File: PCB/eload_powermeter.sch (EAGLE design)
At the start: 78 parts, among them IC1 ADS1115_IC, IC2 SGM8582, IC3 TP4056, IC4 FS312F-G, IC5 MT3608, IC6 FS8205, K2 TXD2SA-4.5V, Q1 BSS123, Q3 BSS123, Q4 IRF520, Q5 BSS123, Q6 IRF520, Q7 IRF520, U1 ATMEGA328P, Y1 16MHz

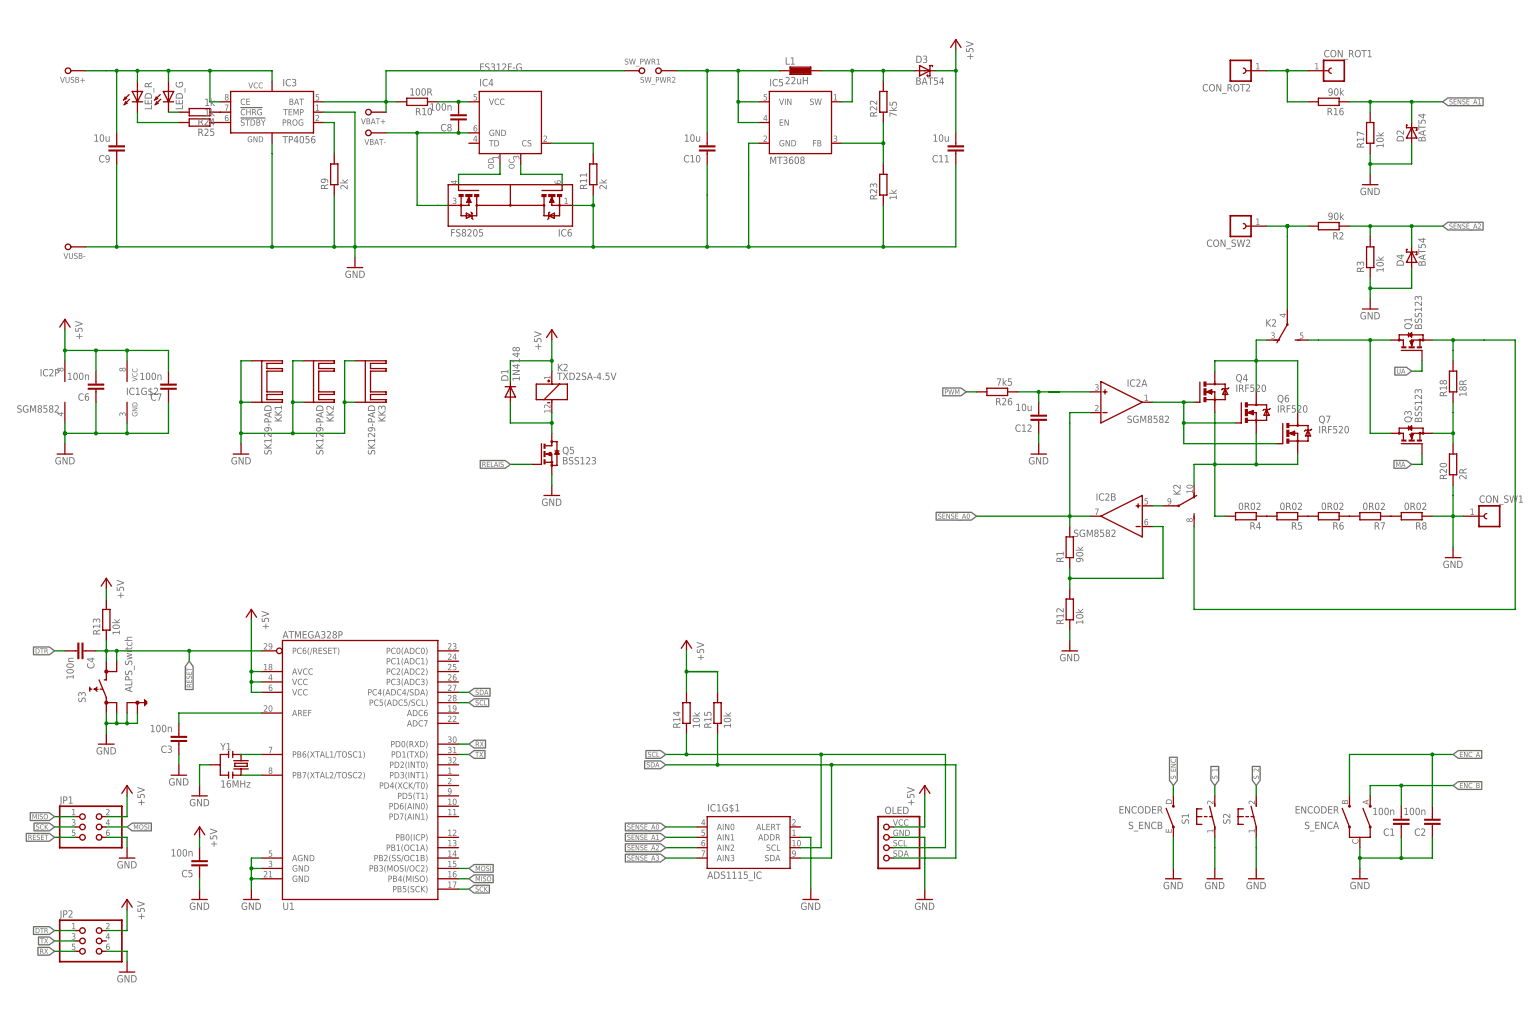
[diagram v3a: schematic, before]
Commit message: Finish Layout, document schematic with blocks
Routing the last connections of the layout. Starting with the naming on the top panel.
Documenting the schematic by adding functional blocks and descriping them.
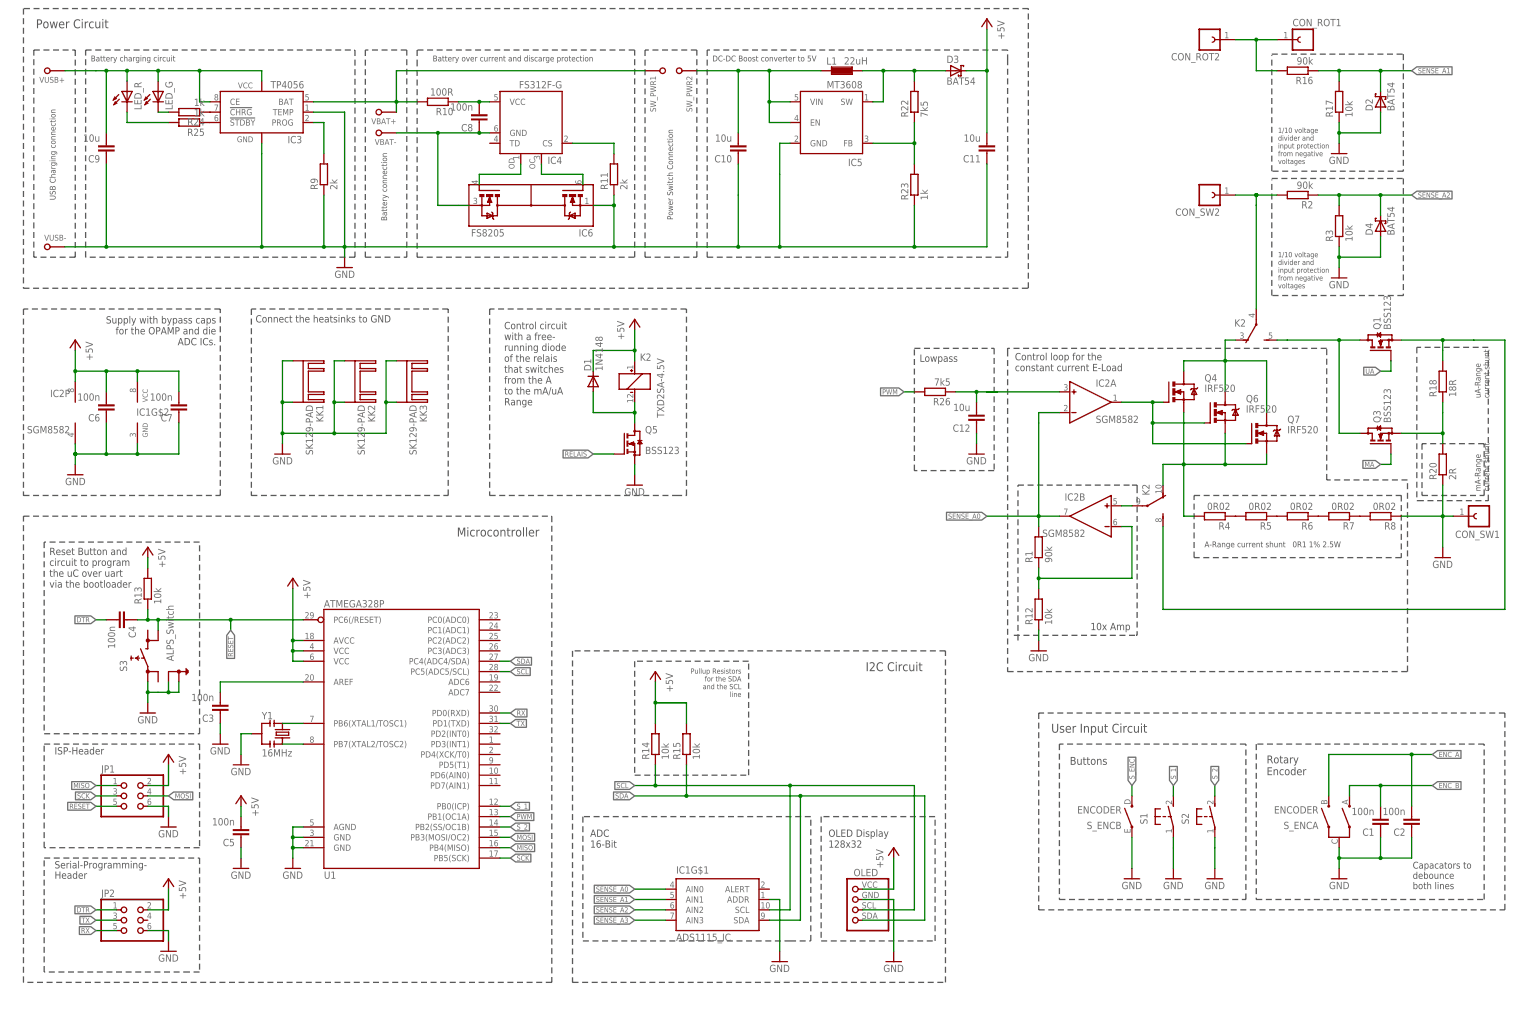
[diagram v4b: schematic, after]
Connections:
- net GND: no longer S3.3.2
- net PWM: now also U1.PB1(OC1A)
- net RESET: no longer S3.4.1
- net S_1: now also U1.PB0(ICP)
- net S_2: now also U1.PB2(SS/OC1B)
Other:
- note added: "1/10 voltage divider and input protection from negative voltages"
- note added: "10x Amp"
- note added: "A-Range current shunt 0R1 1% 2.5W"
- note added: "ADC 16-Bit"
- note added: "Battery charging circuit"
- note added: "Battery connection"
- note added: "Battery over current and discarge protection"
- note added: "Buttons"
- note added: "Capacators to debounce both lines"
- note added: "Connect the heatsinks to GND"
- note added: "Control circuit with a free- running diode of the relais that switches from the A to the mA/uA Range"
- note added: "Control loop for the constant current E-Load"
- note added: "DC-DC Boost converter to 5V"
- note added: "Header"
- note added: "I2C Circuit"
- note added: "ISP-Header"
- note added: "Lowpass"
- note added: "Microcontroller"
- note added: "OLED Display 128x32"
- note added: "Power Circuit"
- note added: "Power Switch Connection"
- note added: "Pullup Resistors for the SDA and the SCL line"
- note added: "Reset Button and circuit to program the uC over uart via the bootloader"
- note added: "Rotary Encoder"
- note added: "Serial-Programming-"
- note added: "Supply with bypass caps for the OPAMP and die ADC ICs."
- note added: "USB Charging connection"
- note added: "User Input Circuit"
- note added: "mA-Range current shunt"
- note added: "uA-Range current shunt"
- moved on the sheet: C1, C10, C11, C12, C2, C3, C4, C5, C6, C7, C8, C9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

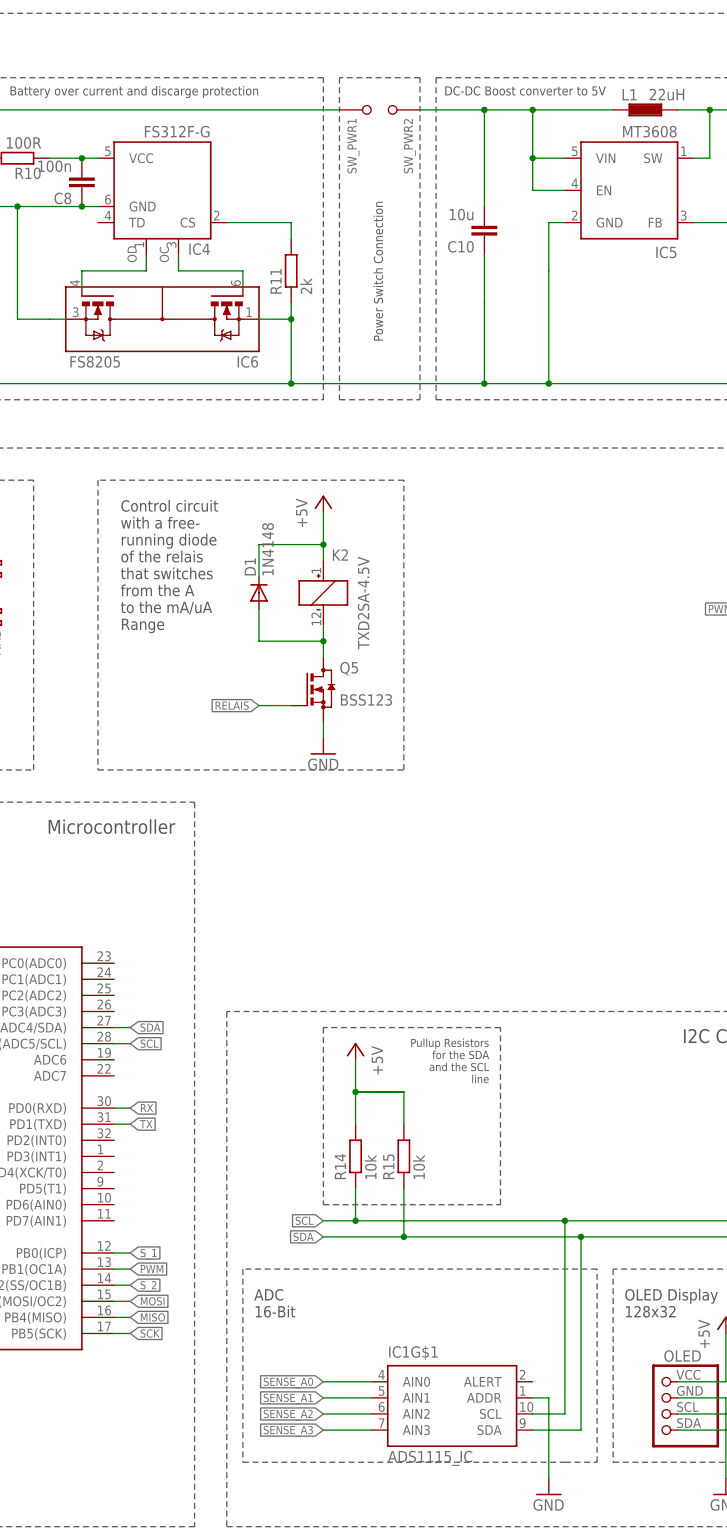
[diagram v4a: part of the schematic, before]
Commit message: Adding some missing uC connections.
Adding some connections of the uC that were missing before.
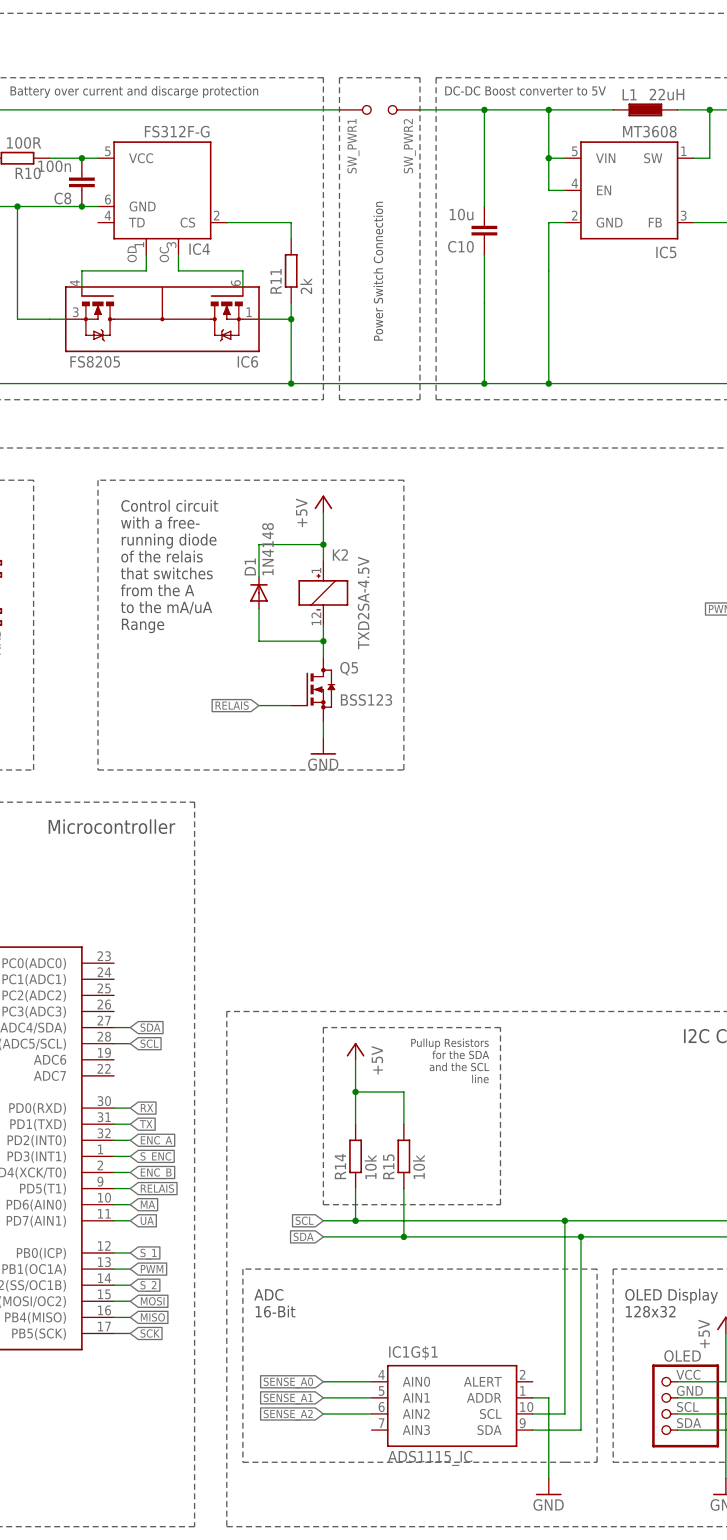
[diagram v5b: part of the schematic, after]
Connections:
- removed net SENSE_A3: IC1G$1.AIN3
- net ENC_A: now also U1.PD2(INT0)
- net ENC_B: now also U1.PD4(XCK/T0)
- net MA: now also U1.PD6(AIN0)
- net RELAIS: now also U1.PD5(T1)
- net S_ENC: now also U1.PD3(INT1)
- net UA: now also U1.PD7(AIN1)
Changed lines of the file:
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@@
 <wire x1="48.26" y1="25.4" x2="48.26" y2="22.86" width="0.1524" layer="91"/>
+</segment>
+<segment>
+<junction x="25.4" y="142.24"/>
 </segment>
 </net>
@@
 <wire x1="167.64" y1="81.28" x2="175.26" y2="81.28" width="0.1524" layer="91"/>
 <pinref part="R15" gate="G$1" pin="2"/>
-<wire x1="175.26" y1="81.28" x2="167.64" y2="81.28" width="0.1524" layer="91"/>
 <wire x1="175.26" y1="76.2" x2="175.26" y2="81.28" width="0.1524" layer="91"/>
 <junction x="167.64" y="81.28"/>
@@
 <wire x1="347.98" y1="162.56" x2="345.44" y2="162.56" width="0.1524" layer="91"/>
 </segment>
+<segment>
+<pinref part="U1" gate="G$1" pin="PD7(AIN1)"/>
+<wire x1="129.54" y1="60.96" x2="132.08" y2="60.96" width="0.1524" layer="91"/>
+<label x="132.08" y="60.96" size="1.27" layer="95" xref="yes"/>
+</segment>
 </net>
 <net name="MA" class="0">
@@
 <wire x1="347.98" y1="139.7" x2="345.44" y2="139.7" width="0.1524" layer="91"/>
 <label x="345.44" y="139.7" size="1.27" layer="95" rot="R180" xref="yes"/>
+</segment>
+<segment>
+<pinref part="U1" gate="G$1" pin="PD6(AIN0)"/>
+<wire x1="129.54" y1="63.5" x2="132.08" y2="63.5" width="0.1524" layer="91"/>
+<label x="132.08" y="63.5" size="1.27" layer="95" xref="yes"/>
 </segment>
 </net>
@@
 </segment>
 </net>
-<net name="SENSE_A3" class="0">
-<segment>
-<wire x1="170.18" y1="27.94" x2="162.56" y2="27.94" width="0.1524" layer="91"/>
-<pinref part="IC1" gate="G$1" pin="AIN3"/>
-<label x="162.56" y="27.94" size="1.27" layer="95" rot="R180" xref="yes"/>
-</segment>
-</net>
 <net name="SENSE_A2" class="0">
 <segment>
@@
 <label x="152.4" y="142.24" size="1.27" layer="95" rot="R180" xref="yes"/>
 </segment>
+<segment>
+<pinref part="U1" gate="G$1" pin="PD5(T1)"/>
+<wire x1="129.54" y1="66.04" x2="132.08" y2="66.04" width="0.1524" layer="91"/>
+<label x="132.08" y="66.04" size="1.27" layer="95" xref="yes"/>
+</segment>
 </net>
 <net name="ENC_B" class="0">
@@
 <label x="358.14" y="60.96" size="1.27" layer="95" xref="yes"/>
 </segment>
+<segment>
+<pinref part="U1" gate="G$1" pin="PD4(XCK/T0)"/>
+<wire x1="129.54" y1="68.58" x2="132.08" y2="68.58" width="0.1524" layer="91"/>
+<label x="132.08" y="68.58" size="1.27" layer="95" xref="yes"/>
+</segment>
 </net>
 <net name="ENC_A" class="0">
@@
 <label x="358.14" y="68.58" size="1.27" layer="95" xref="yes"/>
 </segment>
+<segment>
+<pinref part="U1" gate="G$1" pin="PD2(INT0)"/>
+<wire x1="129.54" y1="73.66" x2="132.08" y2="73.66" width="0.1524" layer="91"/>
+<label x="132.08" y="73.66" size="1.27" layer="95" xref="yes"/>
+</segment>
 </net>
 <net name="S_2" class="0">
@@
 <wire x1="129.54" y1="50.8" x2="132.08" y2="50.8" width="0.1524" layer="91"/>
 <label x="132.08" y="50.8" size="1.27" layer="95" xref="yes"/>
-</segment>
-</net>
-<net name="N$4" class="0">
-<segment>
-<junction x="25.4" y="142.24"/>
 </segment>
 </net>
@@
 <wire x1="187.96" y1="220.98" x2="187.96" y2="236.22" width="0.1524" layer="91"/>
 <pinref part="L1" gate="L" pin="1"/>
-<wire x1="195.58" y1="236.22" x2="208.28" y2="236.22" width="0.1524" layer="91"/>
+<wire x1="198.12" y1="236.22" x2="208.28" y2="236.22" width="0.1524" layer="91"/>
 <pinref part="IC5" gate="G$1" pin="VIN"/>
-<wire x1="195.58" y1="228.6" x2="200.66" y2="228.6" width="0.1524" layer="91"/>
-<junction x="195.58" y="228.6"/>
-<wire x1="195.58" y1="228.6" x2="195.58" y2="236.22" width="0.1524" layer="91"/>
+<wire x1="198.12" y1="228.6" x2="200.66" y2="228.6" width="0.1524" layer="91"/>
+<junction x="198.12" y="228.6"/>
+<wire x1="198.12" y1="228.6" x2="198.12" y2="236.22" width="0.1524" layer="91"/>
 <pinref part="IC5" gate="G$1" pin="EN"/>
-<wire x1="200.66" y1="223.52" x2="195.58" y2="223.52" width="0.1524" layer="91"/>
-<wire x1="195.58" y1="223.52" x2="195.58" y2="228.6" width="0.1524" layer="91"/>
-<wire x1="187.96" y1="236.22" x2="195.58" y2="236.22" width="0.1524" layer="91"/>
-<junction x="195.58" y="236.22"/>
+<wire x1="200.66" y1="223.52" x2="198.12" y2="223.52" width="0.1524" layer="91"/>
+<wire x1="198.12" y1="223.52" x2="198.12" y2="228.6" width="0.1524" layer="91"/>
+<wire x1="187.96" y1="236.22" x2="198.12" y2="236.22" width="0.1524" layer="91"/>
+<junction x="198.12" y="236.22"/>
 <pinref part="SW_PWR2" gate="G$1" pin="P$1"/>
 <wire x1="177.8" y1="236.22" x2="187.96" y2="236.22" width="0.1524" layer="91"/>
@@
 <label x="284.48" y="60.96" size="1.27" layer="95" rot="R90" xref="yes"/>
 </segment>
+<segment>
+<pinref part="U1" gate="G$1" pin="PD3(INT1)"/>
+<wire x1="129.54" y1="71.12" x2="132.08" y2="71.12" width="0.1524" layer="91"/>
+<label x="132.08" y="71.12" size="1.27" layer="95" xref="yes"/>
+</segment>
 </net>
 <net name="SCK" class="0">
@@
 </sheet>
 </sheets>
+<errors>
+</errors>
 </schematic>
 </drawing>
